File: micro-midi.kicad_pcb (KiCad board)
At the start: 2 copper layers, 40 x 27.5 mm, 14 parts, among them J1 AudioJack3, J2 Conn_01x04_Male, J3 AudioJack3, U1 74HC04, U2 6N137

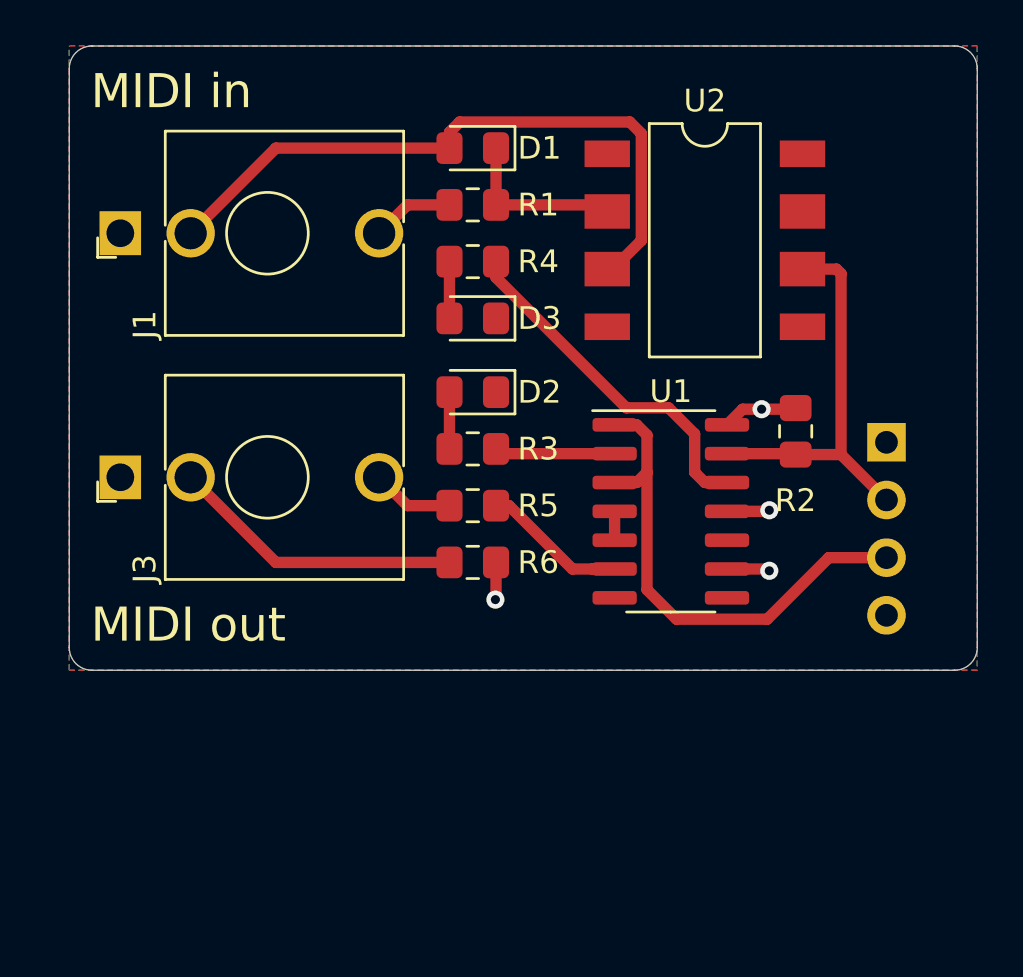
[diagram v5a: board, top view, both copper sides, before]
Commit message: reorder parts to make board more compact
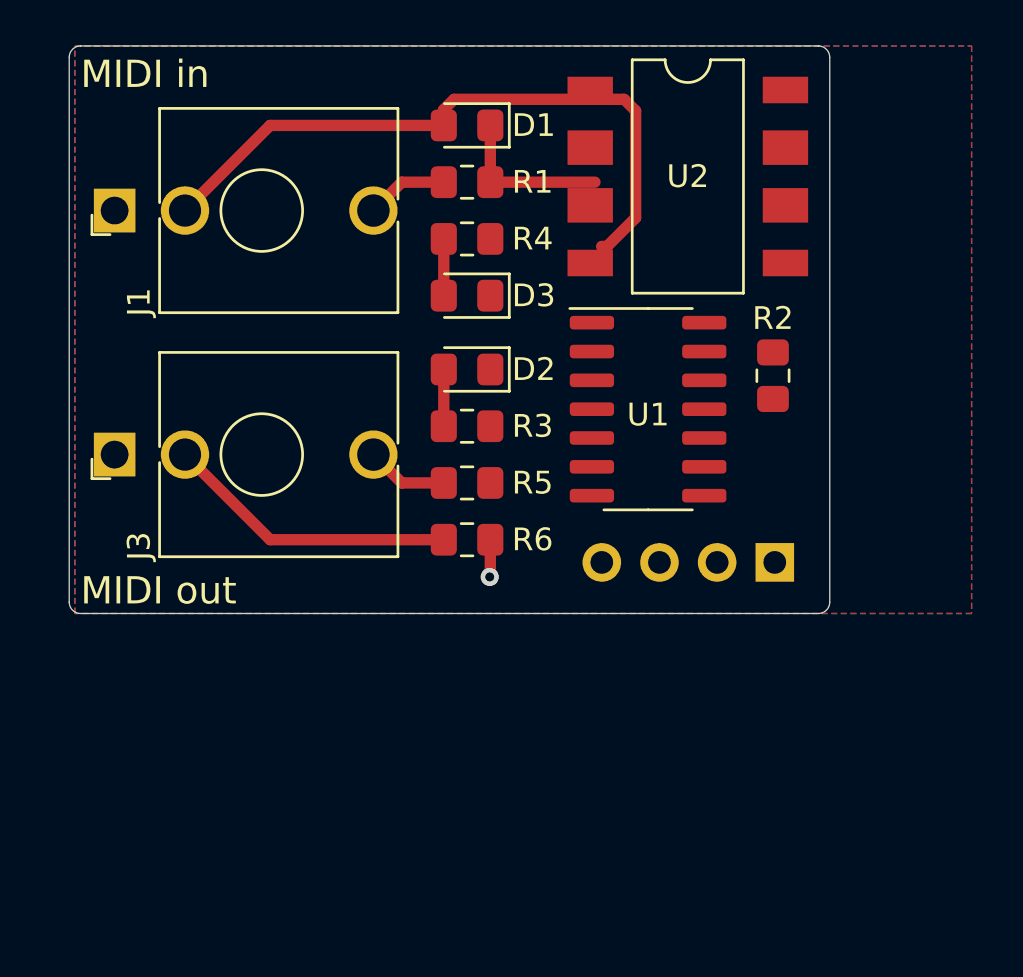
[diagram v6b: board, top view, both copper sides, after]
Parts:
- moved J2 7.22 mm to (101.1, 62.8), turned to 90 degrees
- moved U1 4.61 mm to (95.5, 56.0)
- moved U2 2.91 mm to (97.2, 45.8)
- moved R2 2.65 mm to (101.0, 54.5), turned to 270 degrees
- moved D1 1.03 mm to (87.5, 43.5)
- moved D2 1.03 mm to (87.5, 54.2)
- moved D3 1.03 mm to (87.5, 51.0)
- moved J1 1.03 mm to (72.0, 47.2)
- moved J3 1.03 mm to (72.0, 58.0)
- moved R1 1.03 mm to (87.5, 46.0)
- moved R3 1.03 mm to (87.5, 56.8)
- moved R4 1.03 mm to (87.5, 48.5)
- moved R5 1.03 mm to (87.5, 59.2)
- moved R6 1.03 mm to (87.5, 61.8)
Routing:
- net Net-(J2-Pad3): track 22.2 -> 0.00 mm
- net Net-(J2-Pad2): track 17.6 -> 0.00 mm
- net Net-(R4-Pad2): track 15.6 -> 0.00 mm
- net +5V: track 8.76 -> 1.65 mm, vias 4 -> 1
- net Net-(R5-Pad2): track 6.38 -> 0.00 mm
- net Net-(R3-Pad2): track 5.31 -> 0.30 mm
- net Net-(U1-Pad4): track 1.27 -> 0.00 mm
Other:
- board size 40 x 27.5 mm -> 33.5 x 25 mm

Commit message: clean up copper
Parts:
- moved J2 1.56 mm to (99.5, 62.5)
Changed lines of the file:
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@@
   )
   (module Connector_PinHeader_2.54mm:PinHeader_1x04_P2.54mm_Vertical (layer B.Cu)
-    (at 101.08 62.75 90)
+    (at 99.54 62.5 90)
     (descr "Through hole straight pin header, 1x04, 2.54mm pitch, single row")
     (tags "Through hole pin header THT 1x04 2.54mm single row")
@@
     (polygon
       (pts
-        (xy 109.75 65) (xy 70.25 65) (xy 70.25 40) (xy 109.75 40)
+        (xy 103.5 65) (xy 70 65) (xy 70 40) (xy 103.5 40)
       )
     )
@@
     (polygon
       (pts
-        (xy 109.75 65) (xy 70.25 65) (xy 70.25 40) (xy 109.75 40)
+        (xy 103.5 65) (xy 70.25 65) (xy 70.25 40) (xy 103.5 40)
       )
     )

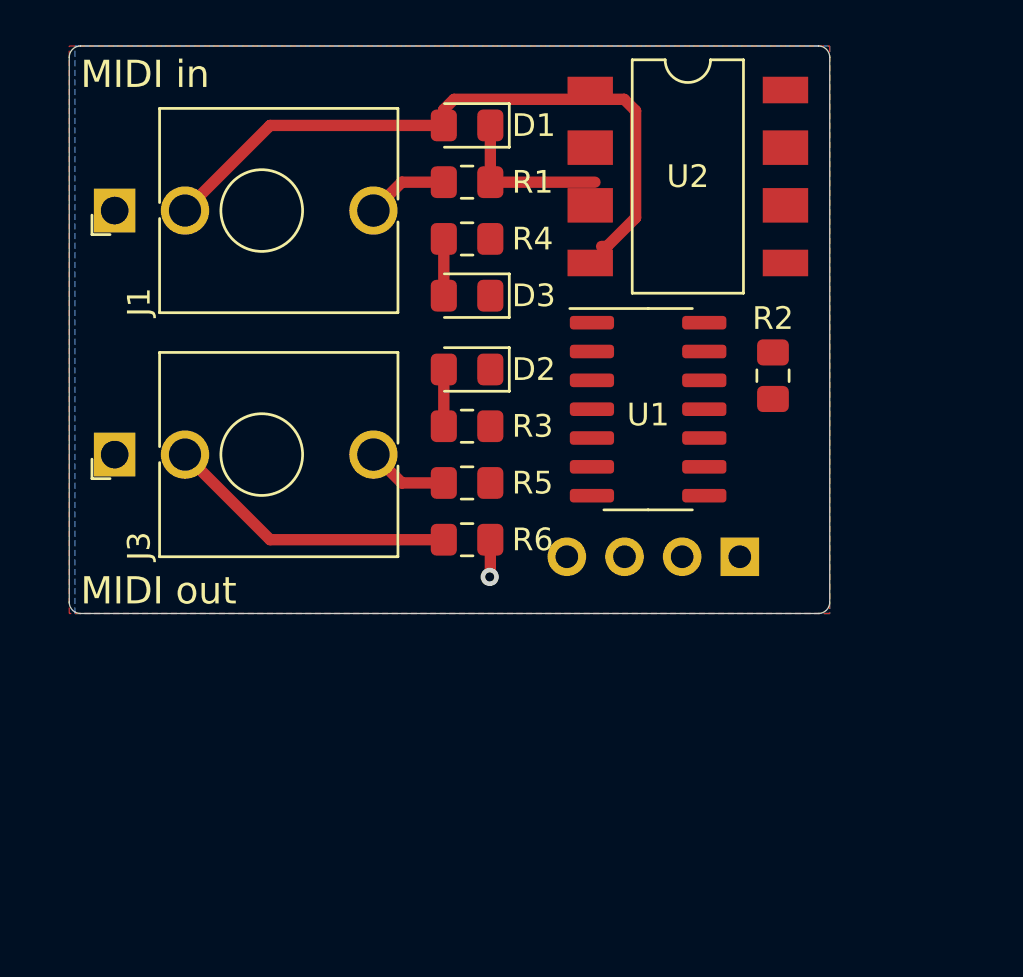
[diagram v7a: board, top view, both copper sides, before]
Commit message: change back copper fill to gnd and re-route board
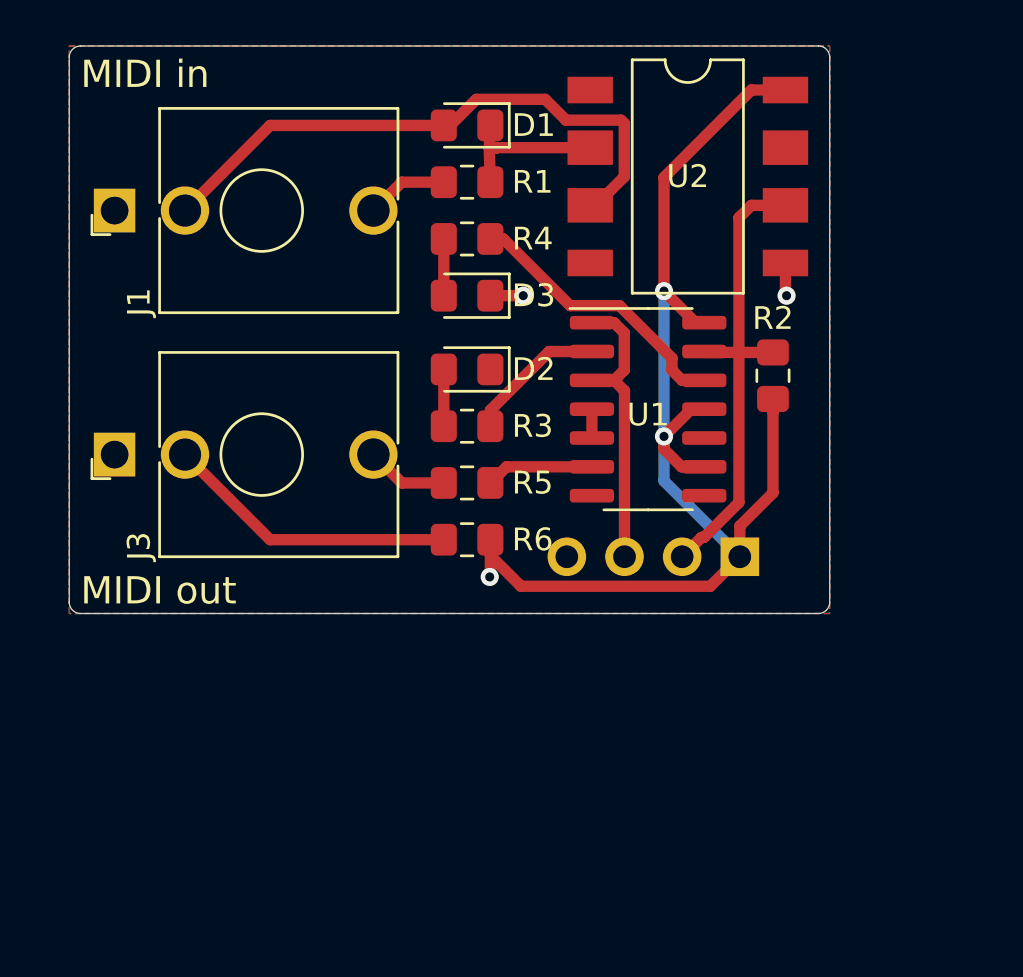
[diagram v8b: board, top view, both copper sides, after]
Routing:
- net +5V: track 1.65 -> 54.3 mm, vias 1 -> 3
- net Net-(J2-Pad2): track 0.00 -> 21.3 mm
- net Net-(J2-Pad3): track 0.00 -> 12.8 mm
- net Net-(R4-Pad2): track 0.00 -> 12.3 mm
- net Net-(R3-Pad2): track 0.30 -> 6.54 mm
- net Net-(R5-Pad2): track 0.00 -> 4.77 mm
- net Net-(D1-Pad2): track 29.2 -> 26.2 mm
- net GND: track 0.00 -> 2.91 mm, vias 0 -> 2
- net Net-(U1-Pad4): track 0.00 -> 1.27 mm
- added copper zone on B.Cu, net GND
- removed copper zone on B.Cu, net +5V
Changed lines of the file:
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@@
     (thickness 1.6)
     (drawings 10)
-    (tracks 23)
+    (tracks 87)
     (zones 0)
     (modules 14)
@@
   (page A4)
   (layers
-    (0 F.Cu signal hide)
+    (0 F.Cu signal)
     (31 B.Cu signal hide)
     (32 B.Adhes user)
@@
     (user_trace_width 0.5)
     (trace_clearance 0.2)
-    (zone_clearance 0.508)
+    (zone_clearance 0.1)
     (zone_45_only no)
     (trace_min 0.2)
@@
   (segment (start 86.5 43.5) (end 78.85 43.5) (width 0.5) (layer F.Cu) (net 1) (status 10))
   (segment (start 78.85 43.5) (end 75.1 47.25) (width 0.5) (layer F.Cu) (net 1) (status 20))
-  (segment (start 93.45 48.83) (end 93.69 48.83) (width 0.5) (layer F.Cu) (net 1))
-  (segment (start 93.69 48.83) (end 94.95 47.57) (width 0.5) (layer F.Cu) (net 1))
-  (segment (start 94.95 47.57) (end 94.95 42.854998) (width 0.5) (layer F.Cu) (net 1))
-  (segment (start 94.95 42.854998) (end 94.444992 42.34999) (width 0.5) (layer F.Cu) (net 1))
-  (segment (start 94.444992 42.34999) (end 86.95001 42.34999) (width 0.5) (layer F.Cu) (net 1))
-  (segment (start 86.95001 42.34999) (end 86.5 42.8) (width 0.5) (layer F.Cu) (net 1) (status 20))
-  (segment (start 86.5 42.8) (end 86.5 43.5) (width 0.5) (layer F.Cu) (net 1) (status 30))
-  (segment (start 88.55 46) (end 88.55 43.5) (width 0.5) (layer F.Cu) (net 2) (status 30))
-  (segment (start 88.55 46) (end 93.16 46) (width 0.5) (layer F.Cu) (net 2) (status 30))
+  (segment (start 93.19 47.02) (end 92.95 47.02) (width 0.5) (layer F.Cu) (net 1))
+  (segment (start 94.45 45.76) (end 93.19 47.02) (width 0.5) (layer F.Cu) (net 1))
+  (segment (start 94.45 43.409998) (end 94.45 45.76) (width 0.5) (layer F.Cu) (net 1))
+  (segment (start 94.310001 43.269999) (end 94.45 43.409998) (width 0.5) (layer F.Cu) (net 1))
+  (segment (start 91.884997 43.269999) (end 94.310001 43.269999) (width 0.5) (layer F.Cu) (net 1))
+  (segment (start 90.964988 42.34999) (end 91.884997 43.269999) (width 0.5) (layer F.Cu) (net 1))
+  (segment (start 87.935044 42.34999) (end 90.964988 42.34999) (width 0.5) (layer F.Cu) (net 1))
+  (segment (start 86.785034 43.5) (end 87.935044 42.34999) (width 0.5) (layer F.Cu) (net 1))
+  (segment (start 86.5 43.5) (end 86.785034 43.5) (width 0.5) (layer F.Cu) (net 1))
+  (segment (start 88.83 44.48) (end 88.81 44.5) (width 0.5) (layer F.Cu) (net 2))
+  (segment (start 92.95 44.48) (end 88.83 44.48) (width 0.5) (layer F.Cu) (net 2))
+  (segment (start 88.55 46) (end 88.5 44.5) (width 0.5) (layer F.Cu) (net 2))
+  (segment (start 88.81 44.5) (end 88.5 44.5) (width 0.5) (layer F.Cu) (net 2))
+  (segment (start 88.5 44.5) (end 88.55 43.5) (width 0.5) (layer F.Cu) (net 2))
   (segment (start 88.55 63.362) (end 88.523 63.389) (width 0.5) (layer F.Cu) (net 3))
   (segment (start 88.55 61.75) (end 88.55 63.362) (width 0.5) (layer F.Cu) (net 3) (status 10))
   (via (at 88.523 63.389) (size 0.8) (drill 0.4) (layers F.Cu B.Cu) (net 3))
+  (segment (start 101 56.125) (end 101 55.55) (width 0.5) (layer F.Cu) (net 3))
+  (segment (start 101 59.69) (end 101 56.125) (width 0.5) (layer F.Cu) (net 3))
+  (segment (start 99.54 61.15) (end 101 59.69) (width 0.5) (layer F.Cu) (net 3))
+  (segment (start 99.54 62.5) (end 99.54 61.15) (width 0.5) (layer F.Cu) (net 3))
+  (segment (start 88.55 62.45) (end 88.55 61.75) (width 0.5) (layer F.Cu) (net 3))
+  (segment (start 98.239999 63.800001) (end 89.900001 63.800001) (width 0.5) (layer F.Cu) (net 3))
+  (segment (start 89.900001 63.800001) (end 88.55 62.45) (width 0.5) (layer F.Cu) (net 3))
+  (segment (start 99.54 62.5) (end 98.239999 63.800001) (width 0.5) (layer F.Cu) (net 3))
+  (segment (start 98.015 53.5) (end 97.975 53.46) (width 0.5) (layer F.Cu) (net 4))
+  (segment (start 99.5 60.108544) (end 99.5 53.5) (width 0.5) (layer F.Cu) (net 4))
+  (segment (start 97.849999 61.650001) (end 97.958543 61.650001) (width 0.5) (layer F.Cu) (net 4))
+  (segment (start 97 62.5) (end 97.849999 61.650001) (width 0.5) (layer F.Cu) (net 4))
+  (segment (start 101 53.5) (end 99.5 53.5) (width 0.5) (layer F.Cu) (net 4))
+  (segment (start 97.958543 61.650001) (end 99.5 60.108544) (width 0.5) (layer F.Cu) (net 4))
+  (segment (start 99.5 53.5) (end 98.015 53.5) (width 0.5) (layer F.Cu) (net 4))
+  (segment (start 100.05 47.02) (end 99.5 47.57) (width 0.5) (layer F.Cu) (net 4))
+  (segment (start 99.5 47.57) (end 99.5 53.5) (width 0.5) (layer F.Cu) (net 4))
+  (segment (start 101.55 47.02) (end 100.05 47.02) (width 0.5) (layer F.Cu) (net 4))
+  (via (at 96.2 57.2) (size 0.8) (drill 0.4) (layers F.Cu B.Cu) (net 3))
+  (segment (start 96.2 59.16) (end 99.54 62.5) (width 0.5) (layer B.Cu) (net 3))
+  (segment (start 96.2 57.2) (end 96.2 59.16) (width 0.5) (layer B.Cu) (net 3))
+  (segment (start 97.4 56) (end 96.2 57.2) (width 0.5) (layer F.Cu) (net 3))
+  (segment (start 97.975 56) (end 97.4 56) (width 0.5) (layer F.Cu) (net 3))
+  (segment (start 96.2 57.765685) (end 96.2 57.2) (width 0.5) (layer F.Cu) (net 3))
+  (segment (start 96.974315 58.54) (end 96.2 57.765685) (width 0.5) (layer F.Cu) (net 3))
+  (segment (start 97.975 58.54) (end 96.974315 58.54) (width 0.5) (layer F.Cu) (net 3))
+  (via (at 96.2 50.8) (size 0.8) (drill 0.4) (layers F.Cu B.Cu) (net 3))
+  (segment (start 96.2 57.2) (end 96.2 50.8) (width 0.5) (layer B.Cu) (net 3))
+  (segment (start 100.05 41.94) (end 101.55 41.94) (width 0.5) (layer F.Cu) (net 3))
+  (segment (start 96.2 45.79) (end 100.05 41.94) (width 0.5) (layer F.Cu) (net 3))
+  (segment (start 96.2 50.8) (end 96.2 45.79) (width 0.5) (layer F.Cu) (net 3))
+  (segment (start 97.59 52.19) (end 96.2 50.8) (width 0.5) (layer F.Cu) (net 3))
+  (segment (start 97.975 52.19) (end 97.59 52.19) (width 0.5) (layer F.Cu) (net 3))
+  (via (at 90 51) (size 0.8) (drill 0.4) (layers F.Cu B.Cu) (net 5))
+  (segment (start 88.55 51) (end 90 51) (width 0.5) (layer F.Cu) (net 5))
+  (segment (start 101.55 49.56) (end 101.55 50.95) (width 0.5) (layer F.Cu) (net 5))
+  (via (at 101.6 51) (size 0.8) (drill 0.4) (layers F.Cu B.Cu) (net 5))
+  (segment (start 101.55 50.95) (end 101.6 51) (width 0.5) (layer F.Cu) (net 5))
   (segment (start 84.65 46) (end 86.5 46) (width 0.5) (layer F.Cu) (net 6) (status 20))
   (segment (start 83.4 47.25) (end 84.65 46) (width 0.5) (layer F.Cu) (net 6) (status 10))
   (segment (start 86.5 54.25) (end 86.5 56.75) (width 0.5) (layer F.Cu) (net 7) (status 30))
   (segment (start 86.5 51) (end 86.5 48.5) (width 0.5) (layer F.Cu) (net 8) (status 30))
+  (segment (start 94.45001 54.27999) (end 94 54.73) (width 0.5) (layer F.Cu) (net 9))
+  (segment (start 94.45001 52.64001) (end 94.45001 54.27999) (width 0.5) (layer F.Cu) (net 9))
+  (segment (start 94 52.19) (end 94.45001 52.64001) (width 0.5) (layer F.Cu) (net 9))
+  (segment (start 93.025 52.19) (end 94 52.19) (width 0.5) (layer F.Cu) (net 9))
+  (segment (start 94 54.73) (end 93.025 54.73) (width 0.5) (layer F.Cu) (net 9))
+  (segment (start 94.46 55.19) (end 94 54.73) (width 0.5) (layer F.Cu) (net 9))
+  (segment (start 94.46 62.5) (end 94.46 55.19) (width 0.5) (layer F.Cu) (net 9))
   (segment (start 84.65 59.25) (end 86.5 59.25) (width 0.5) (layer F.Cu) (net 10) (status 20))
   (segment (start 83.4 58) (end 84.65 59.25) (width 0.5) (layer F.Cu) (net 10) (status 10))
   (segment (start 88.76 56.96) (end 88.55 56.75) (width 0.5) (layer F.Cu) (net 11) (status 30))
+  (segment (start 88.55 56.05) (end 91.14 53.46) (width 0.5) (layer F.Cu) (net 11))
+  (segment (start 92.05 53.46) (end 93.025 53.46) (width 0.5) (layer F.Cu) (net 11))
+  (segment (start 91.14 53.46) (end 92.05 53.46) (width 0.5) (layer F.Cu) (net 11))
+  (segment (start 88.55 56.75) (end 88.55 56.05) (width 0.5) (layer F.Cu) (net 11))
+  (segment (start 97 54.73) (end 97.975 54.73) (width 0.5) (layer F.Cu) (net 12))
+  (segment (start 96.54999 53.750028) (end 96.54999 54.27999) (width 0.5) (layer F.Cu) (net 12))
+  (segment (start 94.239952 51.43999) (end 96.54999 53.750028) (width 0.5) (layer F.Cu) (net 12))
+  (segment (start 92.06499 51.43999) (end 94.239952 51.43999) (width 0.5) (layer F.Cu) (net 12))
+  (segment (start 89.125 48.5) (end 92.06499 51.43999) (width 0.5) (layer F.Cu) (net 12))
+  (segment (start 96.54999 54.27999) (end 97 54.73) (width 0.5) (layer F.Cu) (net 12))
+  (segment (start 88.55 48.5) (end 89.125 48.5) (width 0.5) (layer F.Cu) (net 12))
+  (segment (start 89.26 58.54) (end 93.025 58.54) (width 0.5) (layer F.Cu) (net 13))
+  (segment (start 88.55 59.25) (end 89.26 58.54) (width 0.5) (layer F.Cu) (net 13))
   (segment (start 75.1 58) (end 78.85 61.75) (width 0.5) (layer F.Cu) (net 14) (status 10))
   (segment (start 78.85 61.75) (end 86.5 61.75) (width 0.5) (layer F.Cu) (net 14) (status 20))
+  (segment (start 93.025 57.27) (end 93.025 56) (width 0.5) (layer F.Cu) (net 15))
   (zone (net 5) (net_name GND) (layer F.Cu) (hatch edge 0.508)
+    (connect_pads (clearance 0.1))
+    (min_thickness 0.1)
+    (fill yes (arc_segments 32) (thermal_gap 0.508) (thermal_bridge_width 0.508))
+    (polygon
+      (pts
+        (xy 103.5 65) (xy 70 65) (xy 70 40) (xy 103.5 40)
+      )
+    )
+  )
+  (zone (net 5) (net_name GND) (layer B.Cu) (hatch edge 0.508)
     (connect_pads (clearance 0.508))
     (min_thickness 0.254)
@@
       )
     )
-  )
-  (zone (net 3) (net_name +5V) (layer B.Cu) (hatch edge 0.508)
-    (connect_pads (clearance 0.508))
-    (min_thickness 0.254)
-    (fill yes (arc_segments 32) (thermal_gap 0.508) (thermal_bridge_width 0.508))
-    (polygon
-      (pts
-        (xy 103.5 65) (xy 70.25 65) (xy 70.25 40) (xy 103.5 40)
-      )
-    )
